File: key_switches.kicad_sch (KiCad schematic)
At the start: 52 parts, among them SW1 SW_Push, SW10 SW_Push, SW11 SW_Push, SW12 SW_Push, SW13 SW_Push, SW14 SW_Push, SW15 SW_Push, SW16 SW_Push, SW17 SW_Push, SW18 SW_Push, SW19 SW_Push, SW2 SW_Push, SW20 SW_Push, SW21 SW_Push, SW22 SW_Push, SW23 SW_Push, SW24 SW_Push, SW25 SW_Push, SW26 SW_Push, SW3 SW_Push, SW4 SW_Push, SW5 SW_Push, SW6 SW_Push, SW7 SW_Push, SW8 SW_Push, SW9 SW_Push

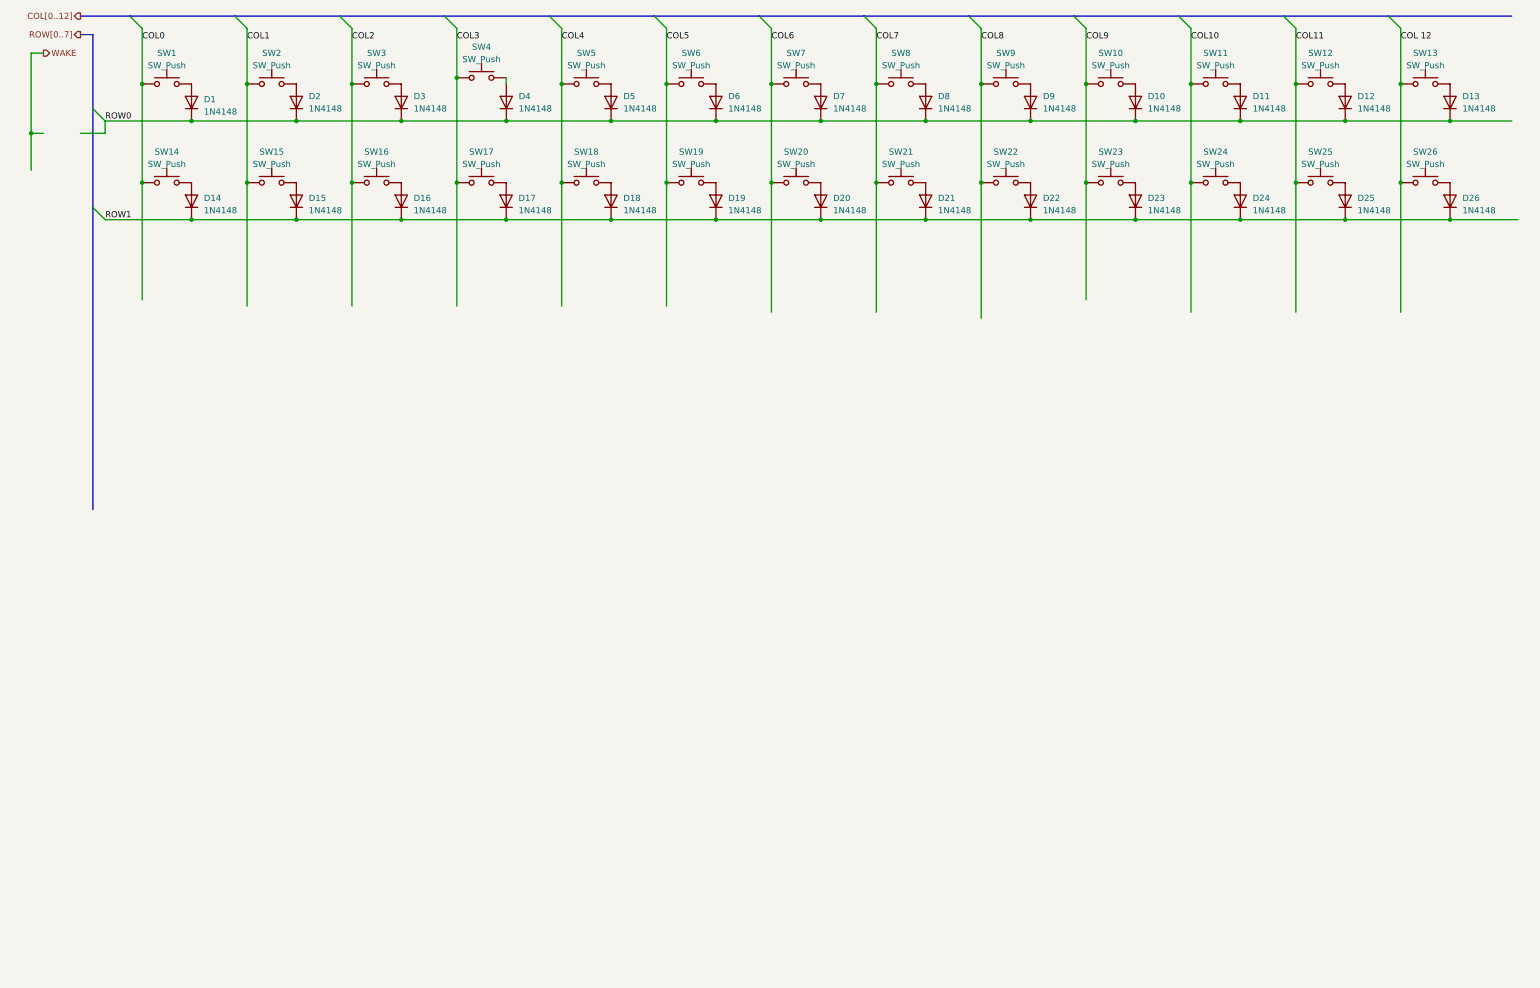
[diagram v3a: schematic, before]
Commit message: a million more keys on row 2
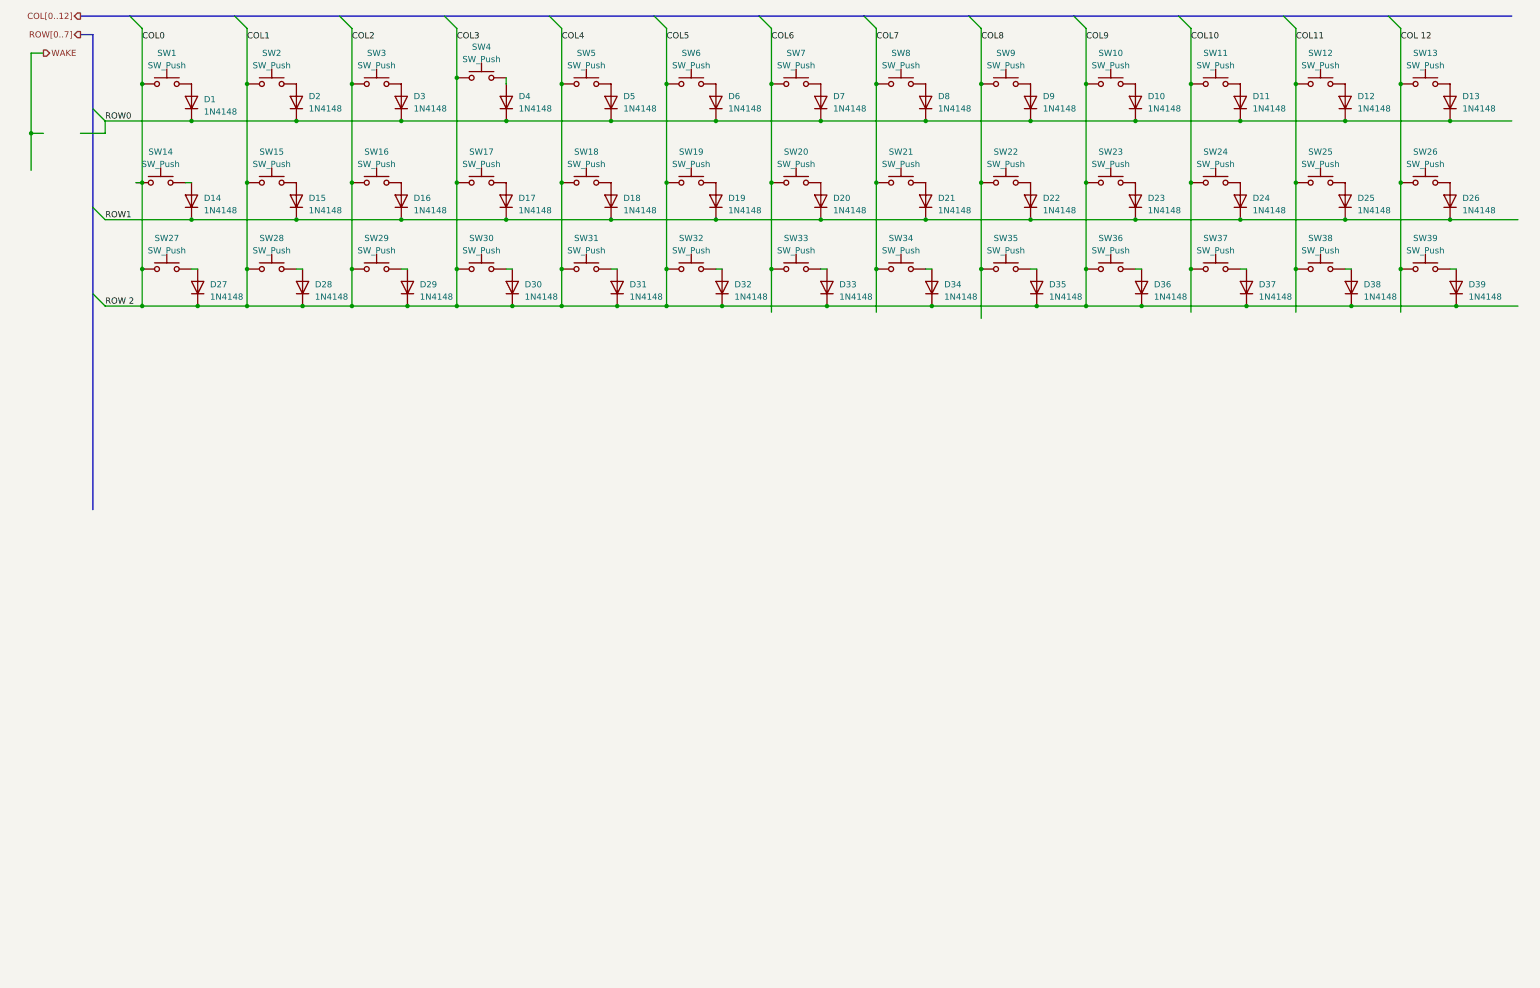
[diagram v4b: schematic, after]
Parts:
- added D27, D28, D29, D30, D31, D32, D33, D34, D35, D36, D37, D38, D39: 1N4148, Diode_THT:D_DO-35_SOD27_P7.62mm_Horizontal, symbol Diode:1N4148
- added SW27, SW28, SW29, SW30, SW31, SW32, SW33, SW34, SW35, SW36, SW37, SW38, SW39: SW_Push, symbol Switch:SW_Push
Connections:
- net COL1 is gone; now on net COL0: SW15.1, SW2.1
- net COL2 is gone; now on net COL0: SW16.1, SW3.1
- net COL3 is gone; now on net COL0: SW17.1, SW4.1
- net COL4 is gone; now on net COL0: SW18.1, SW5.1
- net COL5 is gone; now on net COL0: SW19.1, SW6.1
- net COL9 is gone; now on net COL0: SW10.1, SW23.1
- net COL 12: now also SW39.1
- net COL0: now also D27.1 (K), D28.1 (K), D29.1 (K), D30.1 (K), D31.1 (K), D32.1 (K), D33.1 (K), D34.1 (K), D35.1 (K), D36.1 (K), D37.1 (K), D38.1 (K), D39.1 (K), SW27.1, SW28.1, SW29.1, SW30.1, SW31.1, SW32.1, SW36.1
- net COL10: now also SW37.1
- net COL11: now also SW38.1
- net COL6: now also SW33.1
- net COL7: now also SW34.1
- net COL8: now also SW35.1
- new net: D32.2 (A), SW32.2
- new net: D30.2 (A), SW30.2
- new net: D35.2 (A), SW35.2
- new net: D39.2 (A), SW39.2
- new net: D27.2 (A), SW27.2
- new net: D29.2 (A), SW29.2
- new net: D34.2 (A), SW34.2
- new net: D28.2 (A), SW28.2
- new net: D36.2 (A), SW36.2
- new net: D37.2 (A), SW37.2
- new net: D38.2 (A), SW38.2
- new net: D31.2 (A), SW31.2
- new net: D33.2 (A), SW33.2
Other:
- moved on the sheet: SW14

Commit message: SHOULD BE DONE!!!!!!!
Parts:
- added D100, D101, D102, D103, D104, D40, D41, D42, D43, D44, D45, D46, D47, D48, D49, D50, D51, D52, D53, D54, D55, D56, D57, D58, D59, D60, D61, D62, D63, D64, D65, D66, D67, D68, D69, D70, D71, D72, D73, D74, D75, D76, D77, D78, D79, D80, D81, D82, D83, D84, D85, D86, D87, D88, D89, D90, D91, D92, D93, D94, D95, D96, D97, D98, D99: 1N4148, Diode_THT:D_DO-35_SOD27_P7.62mm_Horizontal, symbol Diode:1N4148
- added SW100, SW101, SW102, SW103, SW104, SW40, SW41, SW42, SW43, SW44, SW45, SW46, SW47, SW48, SW49, SW50, SW51, SW52, SW53, SW54, SW55, SW56, SW57, SW58, SW59, SW60, SW61, SW62, SW63, SW64, SW65, SW66, SW67, SW68, SW69, SW70, SW71, SW72, SW73, SW74, SW75, SW76, SW77, SW78, SW79, SW80, SW81, SW82, SW83, SW84, SW85, SW86, SW87, SW88, SW89, SW90, SW91, SW92, SW93, SW94, SW95, SW96, SW97, SW98, SW99: SW_Push, symbol Switch:SW_Push
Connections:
- net COL 12: now also SW104.1, SW52.1, SW65.1, SW78.1, SW91.1
- net COL0: now also SW101.1, SW40.1, SW41.1, SW42.1, SW43.1, SW44.1, SW45.1, SW49.1, SW53.1, SW54.1, SW55.1, SW56.1, SW57.1, SW58.1, SW62.1, SW66.1, SW67.1, SW68.1, SW69.1, SW70.1, SW71.1, SW75.1, SW79.1, SW80.1, SW81.1, SW82.1, SW83.1, SW84.1, SW88.1, SW92.1, SW93.1, SW94.1, SW95.1, SW96.1, SW97.1
- net COL10: now also SW102.1, SW50.1, SW63.1, SW76.1, SW89.1
- net COL11: now also SW103.1, SW51.1, SW64.1, SW77.1, SW90.1
- net COL6: now also SW46.1, SW59.1, SW72.1, SW85.1, SW98.1
- net COL7: now also SW47.1, SW60.1, SW73.1, SW86.1, SW99.1
- net COL8: now also SW100.1, SW48.1, SW61.1, SW74.1, SW87.1
- new net: D74.2 (A), SW74.2
- new net: D102.2 (A), SW102.2
- new net: D44.2 (A), SW44.2
- new net: D84.2 (A), SW84.2
- new net: D69.2 (A), SW69.2
- new net: D95.2 (A), SW95.2
- new net: D76.2 (A), SW76.2
- new net: D48.2 (A), SW48.2
- new net: D83.2 (A), SW83.2
- new net: D86.2 (A), SW86.2
- new net: D81.2 (A), SW81.2
- new net: D66.2 (A), SW66.2
- new net: D71.2 (A), SW71.2
- new net: D103.2 (A), SW103.2
- new net: D99.2 (A), SW99.2
- new net: D51.2 (A), SW51.2
- new net: D58.2 (A), SW58.2
- new net: D87.2 (A), SW87.2
- new net: D63.2 (A), SW63.2
- new net: D65.2 (A), SW65.2
- new net: D60.2 (A), SW60.2
- new net: D46.2 (A), SW46.2
- new net: D42.2 (A), SW42.2
- new net: D104.2 (A), SW104.2
- new net: D67.2 (A), SW67.2
- new net: D101.2 (A), SW101.2
- new net: D68.2 (A), SW68.2
- new net: D89.2 (A), SW89.2
- new net: D94.2 (A), SW94.2
- new net: D79.2 (A), SW79.2
- new net: D97.2 (A), SW97.2
- new net: D49.2 (A), SW49.2
- new net: D62.2 (A), SW62.2
- new net: D70.2 (A), SW70.2
- new net: D82.2 (A), SW82.2
- new net: D93.2 (A), SW93.2
- new net: D80.2 (A), SW80.2
- new net: D57.2 (A), SW57.2
- new net: D56.2 (A), SW56.2
- new net: D43.2 (A), SW43.2
- new net: D59.2 (A), SW59.2
- new net: D77.2 (A), SW77.2
- new net: D50.2 (A), SW50.2
- new net: D45.2 (A), SW45.2
- new net: D75.2 (A), SW75.2
- new net: D64.2 (A), SW64.2
- new net: D73.2 (A), SW73.2
- new net: D78.2 (A), SW78.2
- new net: D41.2 (A), SW41.2
- new net: D88.2 (A), SW88.2
- new net: D96.2 (A), SW96.2
- new net: D52.2 (A), SW52.2
- new net: D40.2 (A), SW40.2
- new net: D61.2 (A), SW61.2
- new net: D54.2 (A), SW54.2
- new net: D98.2 (A), SW98.2
- new net: D55.2 (A), SW55.2
- new net: D72.2 (A), SW72.2
- new net: D100.2 (A), SW100.2
- new net: D47.2 (A), SW47.2
- new net: D90.2 (A), SW90.2
- new net: D85.2 (A), SW85.2
- new net: D92.2 (A), SW92.2
- new net: D91.2 (A), SW91.2
- new net: D53.2 (A), SW53.2
- new net ROW3: D40.1 (K), D41.1 (K), D42.1 (K), D43.1 (K), D44.1 (K), D45.1 (K), D46.1 (K), D47.1 (K), D48.1 (K), D49.1 (K), D50.1 (K), D51.1 (K), D52.1 (K)
- new net ROW4: D53.1 (K), D54.1 (K), D55.1 (K), D56.1 (K), D57.1 (K), D58.1 (K), D59.1 (K), D60.1 (K), D61.1 (K), D62.1 (K), D63.1 (K), D64.1 (K), D65.1 (K)
- new net ROW5: D66.1 (K), D67.1 (K), D68.1 (K), D69.1 (K), D70.1 (K), D71.1 (K), D72.1 (K), D73.1 (K), D74.1 (K), D75.1 (K), D76.1 (K), D77.1 (K), D78.1 (K)
- new net ROW6: D79.1 (K), D80.1 (K), D81.1 (K), D82.1 (K), D83.1 (K), D84.1 (K), D85.1 (K), D86.1 (K), D87.1 (K), D88.1 (K), D89.1 (K), D90.1 (K), D91.1 (K)
- new net ROW7: D100.1 (K), D101.1 (K), D102.1 (K), D103.1 (K), D104.1 (K), D92.1 (K), D93.1 (K), D94.1 (K), D95.1 (K), D96.1 (K), D97.1 (K), D98.1 (K), D99.1 (K)
